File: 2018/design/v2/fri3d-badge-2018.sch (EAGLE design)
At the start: 138 parts

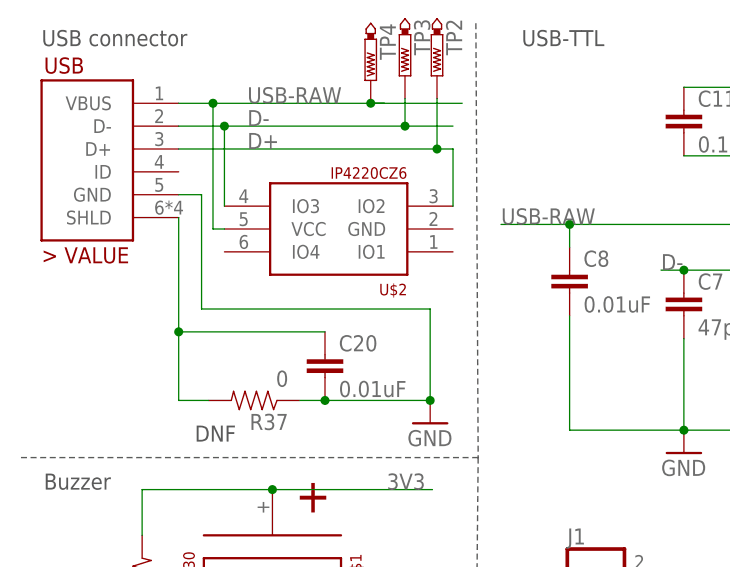
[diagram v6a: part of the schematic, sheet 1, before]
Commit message: further improved USB/ESD/FT traces
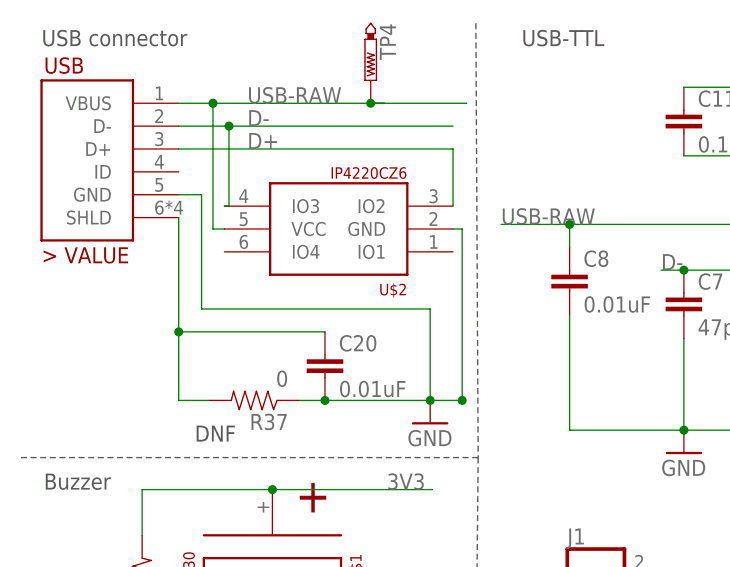
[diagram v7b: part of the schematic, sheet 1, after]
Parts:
- removed TP2, TP3: PTR1B1,27, testpad:PTR1B1,27
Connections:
- net D+: no longer TP2.TP
- net D-: no longer TP3.TP
- net GND: now also U$2.GND
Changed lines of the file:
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@@
 <part name="GND36" library="setup" deviceset="GND" device=""/>
 <part name="TP1" library="testpad" library_urn="urn:adsk.eagle:library:385" deviceset="PTR1" device="B1,27" package3d_urn="urn:adsk.eagle:package:27944/1"/>
-<part name="TP2" library="testpad" library_urn="urn:adsk.eagle:library:385" deviceset="PTR1" device="B1,27" package3d_urn="urn:adsk.eagle:package:27944/1"/>
-<part name="TP3" library="testpad" library_urn="urn:adsk.eagle:library:385" deviceset="PTR1" device="B1,27" package3d_urn="urn:adsk.eagle:package:27944/1"/>
 <part name="TP4" library="testpad" library_urn="urn:adsk.eagle:library:385" deviceset="PTR1" device="B1,27" package3d_urn="urn:adsk.eagle:package:27944/1"/>
 <part name="TP5" library="testpad" library_urn="urn:adsk.eagle:library:385" deviceset="PTR1" device="B1,27" package3d_urn="urn:adsk.eagle:package:27944/1"/>
@@
 <instance part="GND36" gate="1" x="84.074" y="109.728"/>
 <instance part="TP1" gate="G$1" x="113.284" y="168.148"/>
-<instance part="TP2" gate="G$1" x="46.482" y="171.958" rot="R180"/>
-<instance part="TP3" gate="G$1" x="42.926" y="171.958" rot="R180"/>
 <instance part="TP4" gate="G$1" x="39.116" y="171.45" rot="R180"/>
 <instance part="TP5" gate="G$1" x="137.922" y="168.148"/>
@@
 <wire x1="31.242" y1="135.89" x2="34.036" y2="135.89" width="0.1524" layer="91"/>
 <junction x="34.036" y="135.89"/>
+<wire x1="49.53" y1="135.89" x2="49.276" y2="135.89" width="0.1524" layer="91"/>
+<pinref part="U$2" gate="G$1" pin="GND"/>
+<wire x1="49.276" y1="135.89" x2="45.72" y2="135.89" width="0.1524" layer="91"/>
+<wire x1="48.26" y1="154.94" x2="49.276" y2="154.94" width="0.1524" layer="91"/>
+<wire x1="49.276" y1="154.94" x2="49.276" y2="135.89" width="0.1524" layer="91"/>
+<junction x="49.276" y="135.89"/>
 </segment>
 <segment>
@@
 <pinref part="USB" gate="G$1" pin="D+"/>
 <label x="25.4" y="163.83" size="1.778" layer="95"/>
-<wire x1="17.78" y1="163.83" x2="46.482" y2="163.83" width="0.1524" layer="91"/>
-<pinref part="TP2" gate="G$1" pin="TP"/>
-<wire x1="46.482" y1="169.418" x2="46.482" y2="163.83" width="0.1524" layer="91"/>
+<wire x1="17.78" y1="163.83" x2="48.26" y2="163.83" width="0.1524" layer="91"/>
 <pinref part="U$2" gate="G$1" pin="IO2"/>
 <wire x1="48.26" y1="157.48" x2="48.26" y2="163.83" width="0.1524" layer="91"/>
-<wire x1="48.26" y1="163.83" x2="46.482" y2="163.83" width="0.1524" layer="91"/>
-<junction x="46.482" y="163.83"/>
 </segment>
 <segment>
@@
 <label x="25.4" y="166.37" size="1.778" layer="95"/>
 <pinref part="USB" gate="G$1" pin="D-"/>
-<wire x1="17.78" y1="166.37" x2="22.86" y2="166.37" width="0.1524" layer="91"/>
-<pinref part="TP3" gate="G$1" pin="TP"/>
-<wire x1="22.86" y1="166.37" x2="42.926" y2="166.37" width="0.1524" layer="91"/>
-<wire x1="42.926" y1="166.37" x2="48.26" y2="166.37" width="0.1524" layer="91"/>
-<wire x1="42.926" y1="169.418" x2="42.926" y2="166.37" width="0.1524" layer="91"/>
-<junction x="42.926" y="166.37"/>
+<wire x1="17.78" y1="166.37" x2="23.368" y2="166.37" width="0.1524" layer="91"/>
 <pinref part="U$2" gate="G$1" pin="IO3"/>
-<wire x1="22.86" y1="157.48" x2="22.86" y2="166.37" width="0.1524" layer="91"/>
-<junction x="22.86" y="166.37"/>
+<wire x1="23.368" y1="166.37" x2="48.26" y2="166.37" width="0.1524" layer="91"/>
+<wire x1="22.86" y1="157.48" x2="23.368" y2="157.48" width="0.1524" layer="91"/>
+<wire x1="23.368" y1="157.48" x2="23.368" y2="166.37" width="0.1524" layer="91"/>
+<junction x="23.368" y="166.37"/>
 </segment>
 <segment>
@@
 <segment>
 <pinref part="USB" gate="G$1" pin="VBUS"/>
-<wire x1="17.78" y1="168.91" x2="21.59" y2="168.91" width="0.1524" layer="91"/>
 <label x="25.4" y="168.91" size="1.778" layer="95"/>
 <pinref part="TP4" gate="G$1" pin="TP"/>
+<wire x1="17.78" y1="168.91" x2="21.59" y2="168.91" width="0.1524" layer="91"/>
 <wire x1="21.59" y1="168.91" x2="39.116" y2="168.91" width="0.1524" layer="91"/>
 <wire x1="39.116" y1="168.91" x2="40.64" y2="168.91" width="0.1524" layer="91"/>
 <junction x="39.116" y="168.91"/>
-<wire x1="49.276" y1="168.91" x2="39.116" y2="168.91" width="0.1524" layer="91"/>
+<wire x1="49.784" y1="168.91" x2="39.116" y2="168.91" width="0.1524" layer="91"/>
 <pinref part="U$2" gate="G$1" pin="VCC"/>
 <wire x1="22.86" y1="154.94" x2="21.59" y2="154.94" width="0.1524" layer="91"/>

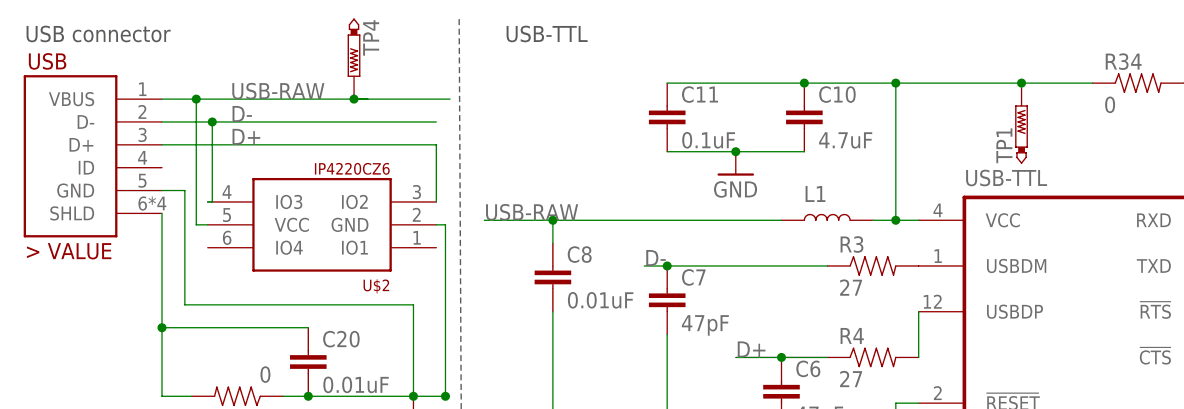
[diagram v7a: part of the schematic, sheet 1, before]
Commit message: redid USB intake again, uncrossing lines at conn
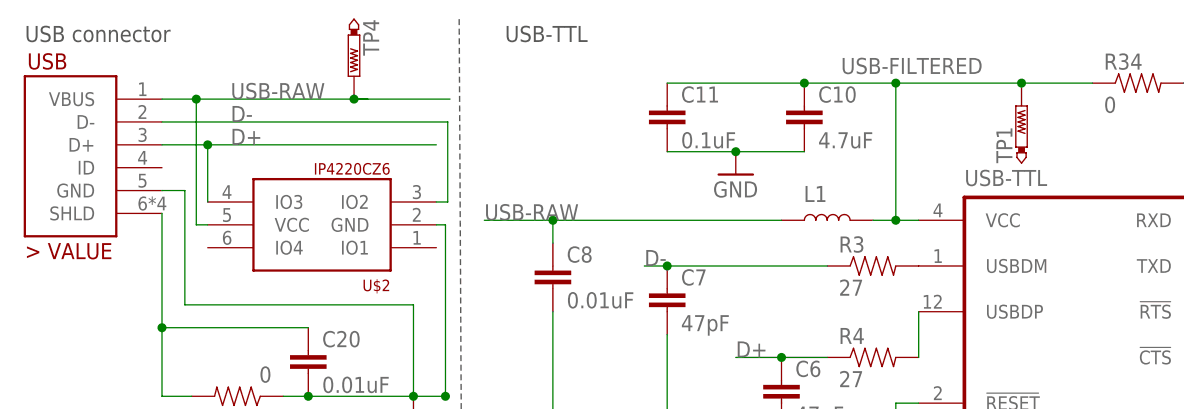
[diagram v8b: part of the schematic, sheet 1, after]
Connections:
- net D+: now also U$2.IO3; no longer U$2.IO2
- net D-: now also U$2.IO2; no longer U$2.IO3
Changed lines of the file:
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@@
 <pinref part="USB" gate="G$1" pin="D+"/>
 <label x="25.4" y="163.83" size="1.778" layer="95"/>
-<wire x1="17.78" y1="163.83" x2="48.26" y2="163.83" width="0.1524" layer="91"/>
-<pinref part="U$2" gate="G$1" pin="IO2"/>
-<wire x1="48.26" y1="157.48" x2="48.26" y2="163.83" width="0.1524" layer="91"/>
+<wire x1="17.78" y1="163.83" x2="22.86" y2="163.83" width="0.1524" layer="91"/>
+<pinref part="U$2" gate="G$1" pin="IO3"/>
+<wire x1="22.86" y1="163.83" x2="48.26" y2="163.83" width="0.1524" layer="91"/>
+<wire x1="22.86" y1="157.48" x2="22.86" y2="163.83" width="0.1524" layer="91"/>
+<junction x="22.86" y="163.83"/>
 </segment>
 <segment>
@@
 <label x="25.4" y="166.37" size="1.778" layer="95"/>
 <pinref part="USB" gate="G$1" pin="D-"/>
-<wire x1="17.78" y1="166.37" x2="23.368" y2="166.37" width="0.1524" layer="91"/>
-<pinref part="U$2" gate="G$1" pin="IO3"/>
-<wire x1="23.368" y1="166.37" x2="48.26" y2="166.37" width="0.1524" layer="91"/>
-<wire x1="22.86" y1="157.48" x2="23.368" y2="157.48" width="0.1524" layer="91"/>
-<wire x1="23.368" y1="157.48" x2="23.368" y2="166.37" width="0.1524" layer="91"/>
-<junction x="23.368" y="166.37"/>
+<wire x1="17.78" y1="166.37" x2="49.53" y2="166.37" width="0.1524" layer="91"/>
+<pinref part="U$2" gate="G$1" pin="IO2"/>
+<wire x1="48.26" y1="157.48" x2="49.53" y2="157.48" width="0.1524" layer="91"/>
+<wire x1="49.53" y1="157.48" x2="49.53" y2="166.37" width="0.1524" layer="91"/>
 </segment>
 <segment>
@@
 <wire x1="113.284" y1="170.688" x2="99.314" y2="170.688" width="0.1524" layer="91"/>
 <junction x="113.284" y="170.688"/>
-</segment>
-</net>
+<label x="93.218" y="171.704" size="1.778" layer="95"/>
+</segment>
+</net>
